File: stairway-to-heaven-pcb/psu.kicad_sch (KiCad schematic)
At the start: 7 parts

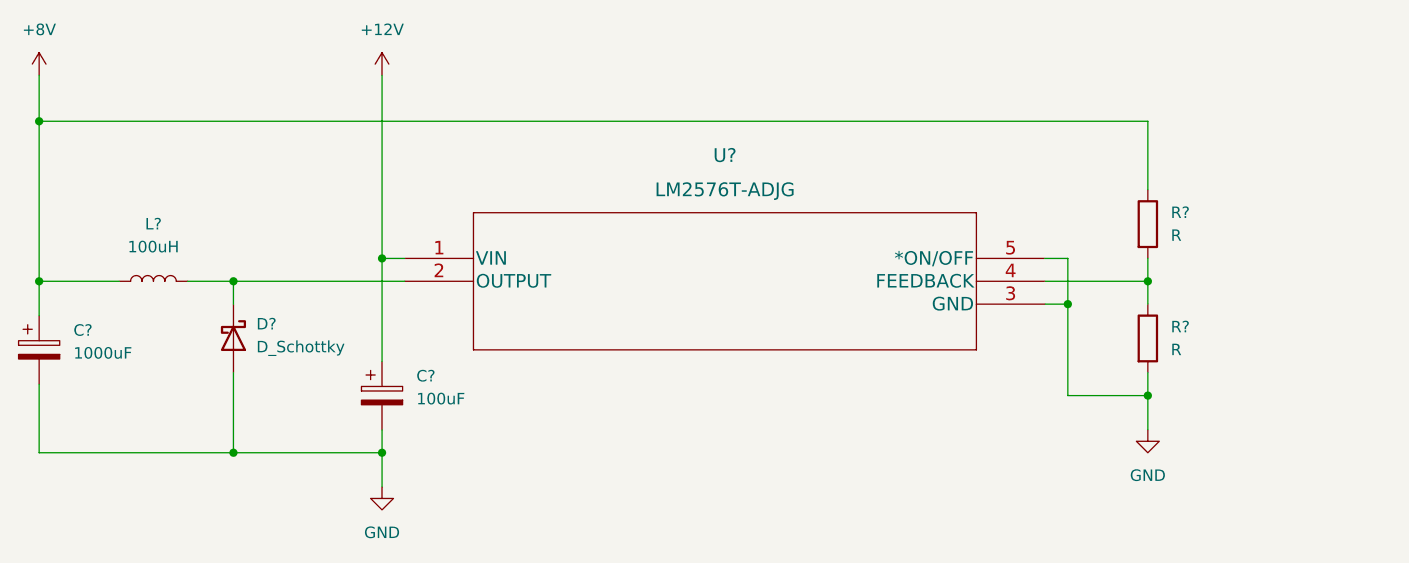
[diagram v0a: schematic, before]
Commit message: DCDC from adj to 5V
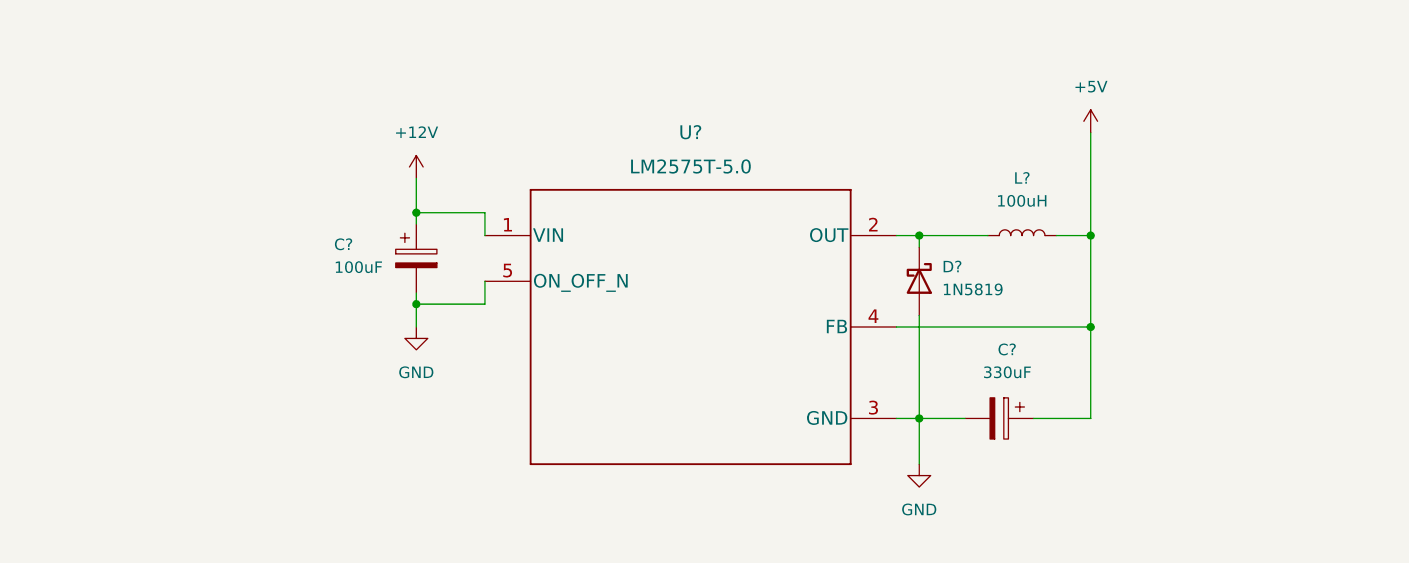
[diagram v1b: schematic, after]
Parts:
- removed D?: D_Schottky, symbol Device:D_Schottky
- removed R? (x2): R, Resistor_SMD:R_0805_2012Metric, symbol Device:R
- removed U?: LM2576T-ADJG, LM2576T-ADJG:LM2576T-ADJG, symbol LM2576T-ADJG:LM2576T-ADJG
- added D?: 1N5819, Diode_THT:D_DO-41_SOD81_P10.16mm_Horizontal, symbol Diode:1N5819
- added U?: LM2575T-5.0, kicad-ss-libs:LM2576T-ADJG, symbol LM2575T-5:LM2575T-5.0
- C?: value 1000uF -> 330uF
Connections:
- net +12V: now also U?.1 (VIN)
- net GND: now also D?.2 (A), U?.3 (GND), U?.5 (ON_OFF_N)
- net +5V: now reaches L?.2
- net +5V: now also C?.1, U?.4 (FB)
- net +8V: no longer names the net of L?.1
- net +8V: now also D?.1 (K), U?.2 (OUT); no longer C?.1
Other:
- moved on the sheet: C?, L?

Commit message: initial pcb placement and routing tests
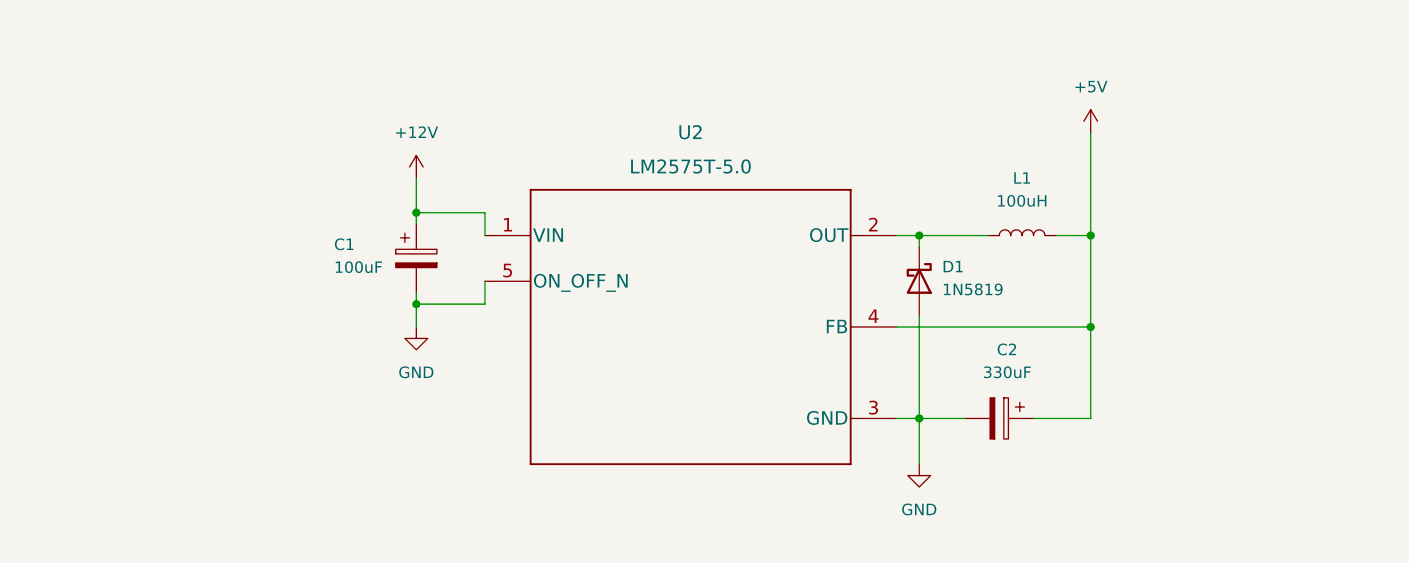
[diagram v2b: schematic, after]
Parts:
- gave numbers to parts that had none: 5
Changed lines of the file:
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@@
   (symbol (lib_id "Device:C_Polarized") (at 118.11 88.9 0) (unit 1)
     (in_bom yes) (on_board yes)
-    (property "Reference" "C?" (id 0) (at 108.966 87.376 0)
+    (property "Reference" "C1" (id 0) (at 108.966 87.376 0)
       (effects (font (size 1.27 1.27)) (justify left))
     )
@@
   (symbol (lib_id "power:+5V") (at 193.04 74.93 0) (unit 1)
     (in_bom yes) (on_board yes) (fields_autoplaced)
-    (property "Reference" "#PWR?" (id 0) (at 193.04 78.74 0)
+    (property "Reference" "#PWR0161" (id 0) (at 193.04 78.74 0)
       (effects (font (size 1.27 1.27)) hide)
     )
@@
   (symbol (lib_id "power:GND") (at 173.99 111.76 0) (unit 1)
     (in_bom yes) (on_board yes) (fields_autoplaced)
-    (property "Reference" "#PWR?" (id 0) (at 173.99 118.11 0)
+    (property "Reference" "#PWR0159" (id 0) (at 173.99 118.11 0)
       (effects (font (size 1.27 1.27)) hide)
     )
@@
   (symbol (lib_id "Device:L") (at 185.42 86.36 90) (unit 1)
     (in_bom yes) (on_board yes) (fields_autoplaced)
-    (property "Reference" "L?" (id 0) (at 185.42 80.01 90))
+    (property "Reference" "L1" (id 0) (at 185.42 80.01 90))
     (property "Value" "100uH" (id 1) (at 185.42 82.55 90))
     (property "Footprint" "" (id 2) (at 185.42 86.36 0)
@@
   (symbol (lib_id "Diode:1N5819") (at 173.99 91.44 270) (unit 1)
     (in_bom yes) (on_board yes) (fields_autoplaced)
-    (property "Reference" "D?" (id 0) (at 176.53 89.8524 90)
+    (property "Reference" "D1" (id 0) (at 176.53 89.8524 90)
       (effects (font (size 1.27 1.27)) (justify left))
     )
@@
   (symbol (lib_id "power:GND") (at 118.11 96.52 0) (unit 1)
     (in_bom yes) (on_board yes) (fields_autoplaced)
-    (property "Reference" "#PWR?" (id 0) (at 118.11 102.87 0)
+    (property "Reference" "#PWR0160" (id 0) (at 118.11 102.87 0)
       (effects (font (size 1.27 1.27)) hide)
     )
@@
   (symbol (lib_id "power:+12V") (at 118.11 80.01 0) (unit 1)
     (in_bom yes) (on_board yes) (fields_autoplaced)
-    (property "Reference" "#PWR?" (id 0) (at 118.11 83.82 0)
+    (property "Reference" "#PWR0162" (id 0) (at 118.11 83.82 0)
       (effects (font (size 1.27 1.27)) hide)
     )
@@
   (symbol (lib_id "Device:C_Polarized") (at 182.88 106.68 270) (unit 1)
     (in_bom yes) (on_board yes) (fields_autoplaced)
-    (property "Reference" "C?" (id 0) (at 183.769 99.06 90))
+    (property "Reference" "C2" (id 0) (at 183.769 99.06 90))
     (property "Value" "330uF" (id 1) (at 183.769 101.6 90))
     (property "Footprint" "" (id 2) (at 179.07 107.6452 0)
@@
   (symbol (lib_id "LM2575T-5:LM2575T-5.0") (at 148.59 96.52 0) (unit 1)
     (in_bom yes) (on_board yes) (fields_autoplaced)
-    (property "Reference" "U?" (id 0) (at 148.59 74.93 0)
+    (property "Reference" "U2" (id 0) (at 148.59 74.93 0)
       (effects (font (size 1.524 1.524)))
     )

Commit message: psu layout
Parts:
- added C3, C5, C6: 10uF, Capacitor_SMD:C_1206_3216Metric, symbol Device:C
- added C4: 100uF, Capacitor_SMD:C_Elec_8x6.2, symbol Device:C_Polarized
- C1: value 100uF -> 47uF; footprint (none) -> Capacitor_SMD:C_Elec_6.3x5.8
- C2: value 330uF -> 100uF; footprint (none) -> Capacitor_SMD:C_Elec_8x6.2
- D1: value 1N5819 -> DO-214AC; footprint Diode_THT:D_DO-41_SOD81_P10.16mm_Horizontal -> Diode_SMD:D_SMA
- L1: footprint (none) -> Inductor_SMD:L_10.4x10.4_H4.8
- U2: footprint kicad-ss-libs:LM2576T-ADJG -> kicad-ss-libs:LM2575T-5.0
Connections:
- net +12V: now also C3.2
- net +5V: now also C4.1, C5.1, C6.1
- net GND: now also C3.1, C4.2, C5.2, C6.2
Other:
- moved on the sheet: C2

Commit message: Silks, small mods
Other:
- title: (none) -> Stairway to Heaven
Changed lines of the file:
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@@
 (kicad_sch (version 20211123) (generator eeschema)
   (paper "A4")
+  (title_block
+    (title "Stairway to Heaven")
+  )
   (junction (at 205.74 106.68) (diameter 0) (color 0 0 0 0)
   )

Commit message: Organize footprints and symbols
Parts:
- U2: footprint kicad-ss-libs:LM2575T-5.0 -> LM2575T-5:LM2575T-5.0
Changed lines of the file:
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@@
       (effects (font (size 1.524 1.524)))
     )
-    (property "Footprint" "kicad-ss-libs:LM2575T-5.0" (id 2) (at 148.59 98.044 0)
+    (property "Footprint" "LM2575T-5:LM2575T-5.0" (id 2) (at 148.59 98.044 0)
       (effects (font (size 1.524 1.524)) hide)
     )
